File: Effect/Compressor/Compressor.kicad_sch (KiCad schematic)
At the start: 46 parts, among them J1 Conn_01x04_Pin, J2 Conn_01x04_Pin, Q1 DMMT5551, Q2 MMBF5103, Q3 DMMT5551, Q4 MMBF5103

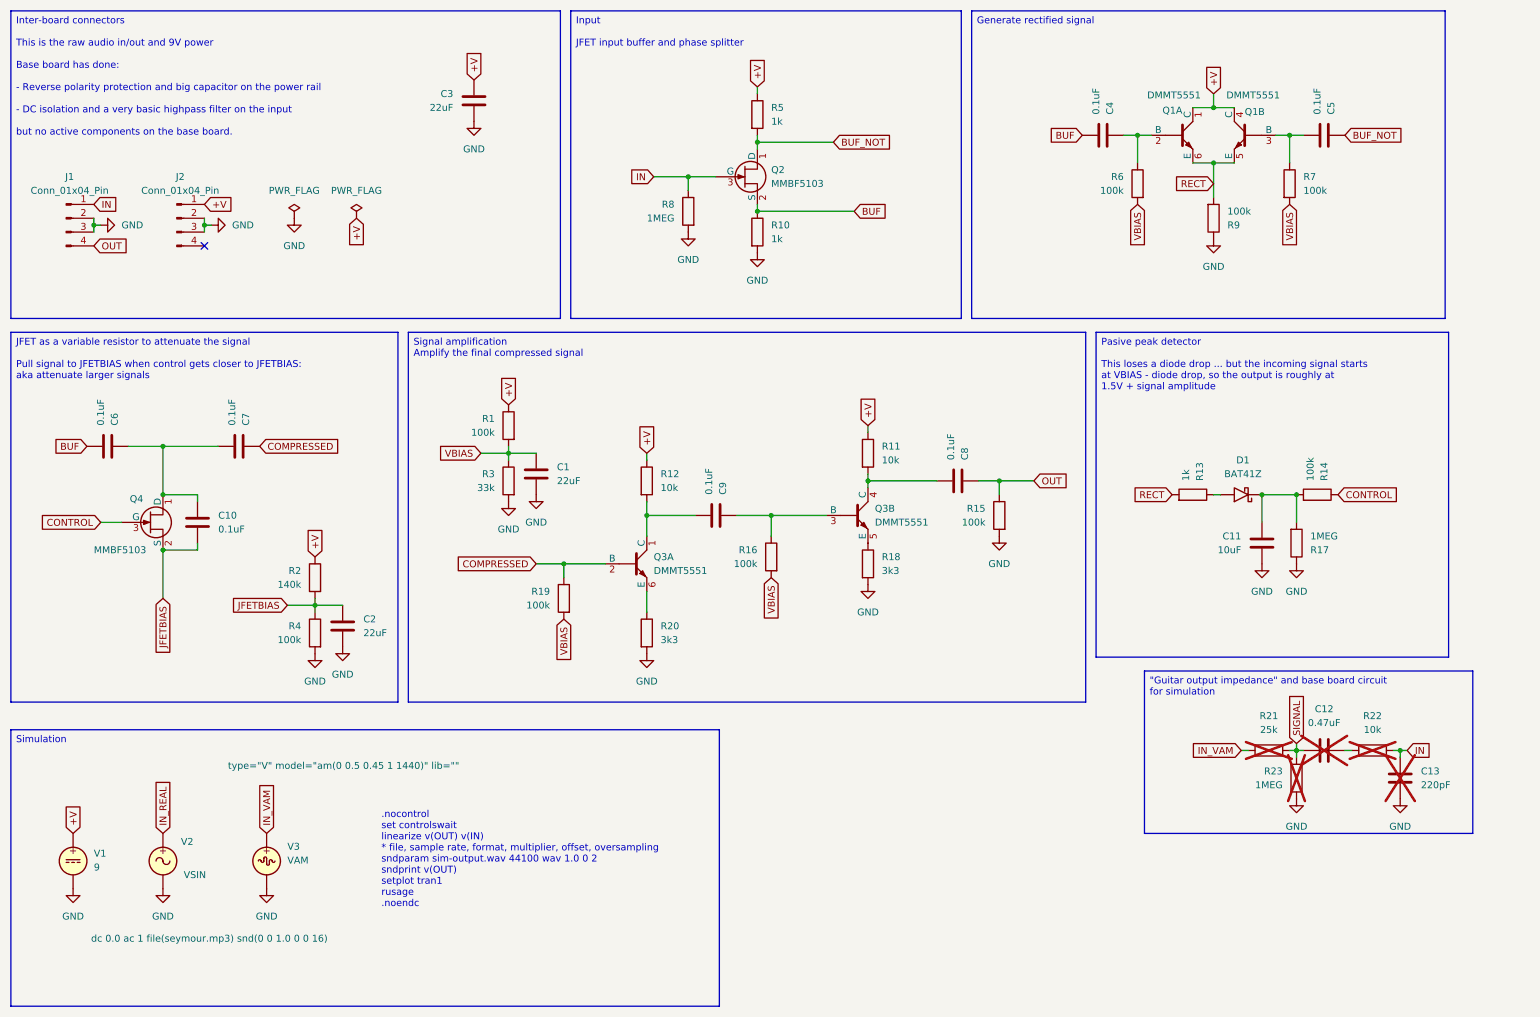
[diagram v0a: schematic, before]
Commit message: Add volume and level pots for compressor
The level pot might make the compressor able to deal with the reality of
JFET variability, at least within reason.

And obviously also in theory then allow people to actually set the level
at which things compress.

It's worth noting that the compression level is set purely based on the
input level. That's really stupid, since it really should be based on
feedback from the *output*, not the input. So high input levels might
then end up compressing to the point that the end result is less than
where medium input levels would have been.

But hey, if this things works even that well, that would be a small
miracle. The much more likely situation is that it will noisy, distort
horribly and not match my simulations at all.

My previous attempts at this do not instill confidence.

So I'll worry about smarter feedback when - and if - I ever get to that
bridge.

This also starts on the PCB layout. No components placed yet, just the
skeleton board with pots and connectors. But it's at the point where I
actually want to know if any of this works in reality, so...

Signed-off-by: Linus Torvalds <torvalds@linux-foundation.org>
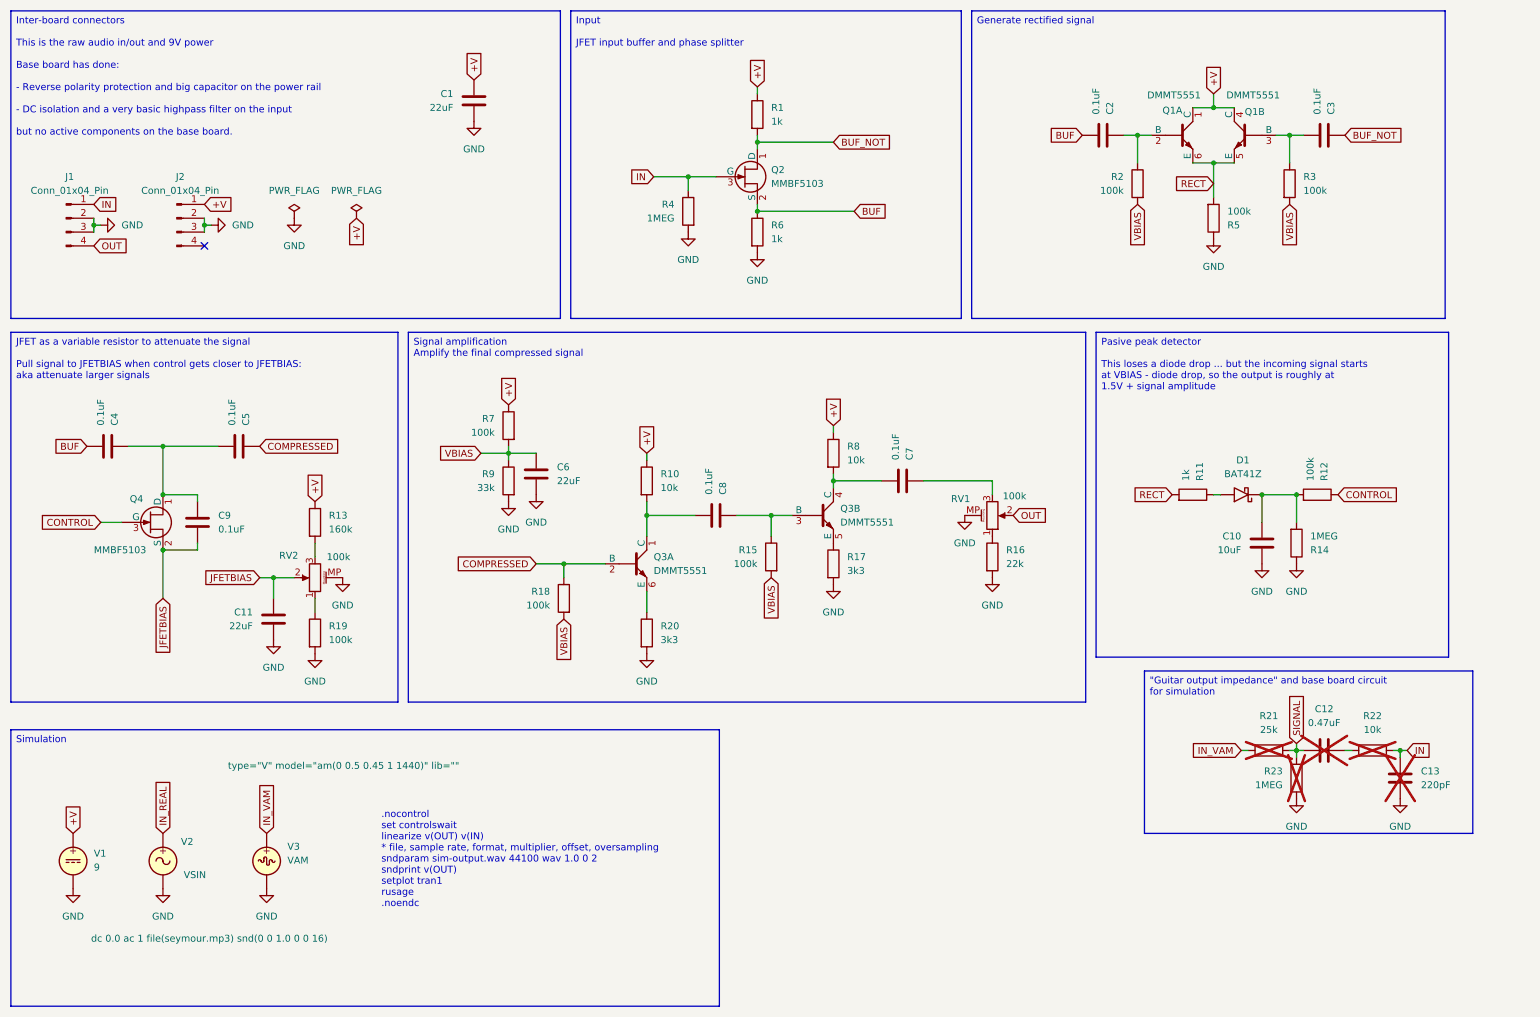
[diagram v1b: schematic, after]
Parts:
- removed R15: 100k, Resistor_SMD:R_0805_2012Metric, symbol Device:R
- added R16: 22k, Resistor_SMD:R_0805_2012Metric, symbol Device:R
- added RV1, RV2: 100k, Mylib:Potentiometer_9mm_MP, symbol Device:R_Potentiometer_MountingPin
- C2: renamed from C4; footprint Capacitor_SMD:C_1206_3216Metric -> Mylib:C_0704_1810Metric
- C3: renamed from C5; footprint Capacitor_SMD:C_1206_3216Metric -> Mylib:C_0704_1810Metric
- C4: renamed from C6; footprint Capacitor_SMD:C_1206_3216Metric -> Mylib:C_0704_1810Metric
- C5: renamed from C7; footprint Capacitor_SMD:C_1206_3216Metric -> Mylib:C_0704_1810Metric
- C7: renamed from C8; footprint Capacitor_SMD:C_1206_3216Metric -> Mylib:C_0704_1810Metric
- C8: renamed from C9; footprint Capacitor_SMD:C_1206_3216Metric -> Mylib:C_0704_1810Metric
- C9: renamed from C10; footprint Capacitor_SMD:C_1206_3216Metric -> Mylib:C_0704_1810Metric
- R13: renamed from R2; value 140k -> 160k
- renumbered C3 to C1, C11 to C10, C2 to C11, C1 to C6, R5 to R1, R12 to R10, R13 to R11, R14 to R12, R17 to R14, R16 to R15, R18 to R17, R19 to R18, R4 to R19, R6 to R2, R7 to R3, R8 to R4, R9 to R5, R10 to R6, R1 to R7, R11 to R8, R3 to R9
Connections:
- net GND: now also R16.2, RV1.MP (MountPin), RV2.MP (MountPin)
- net JFETBIAS: now also RV2.2; no longer R13.2, R19.1
- net OUT: now also RV1.2; no longer C7.1
- new net: R16.1, RV1.1
- new net: R19.1, RV2.1
- new net: R13.2, RV2.3
- new net: C7.1, RV1.3
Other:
- moved on the sheet: C11, C7, Q3B, R13, R17, R8

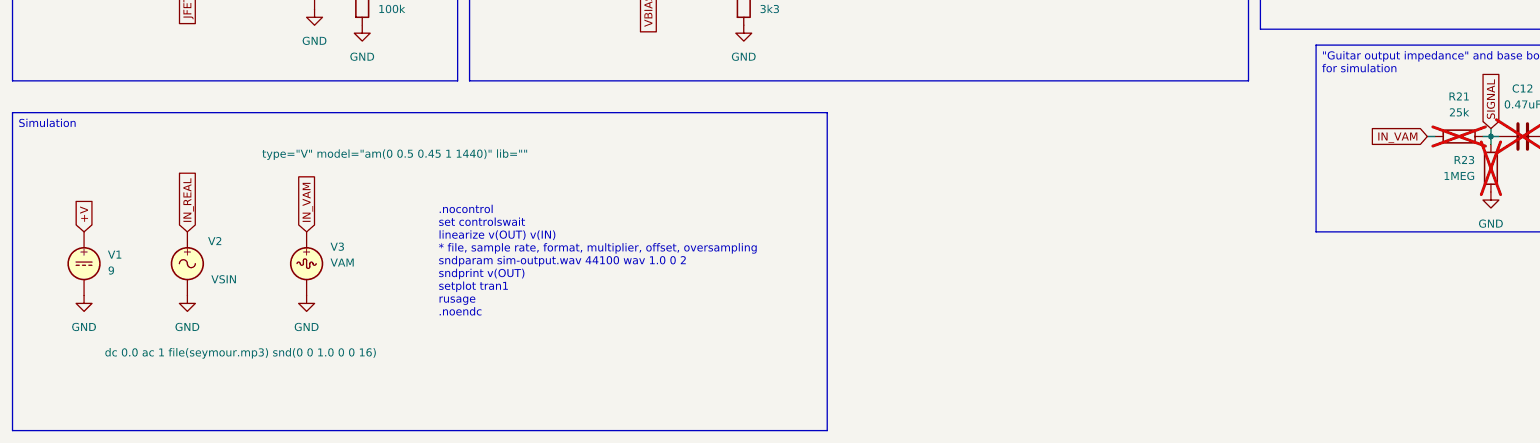
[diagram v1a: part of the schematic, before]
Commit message: Add triangle wave for compressor testing
Because of how this odd "JFET as a voltage-controlled resistor in
parallel with a capacitor" circuit works, the whole ngspice AC signal
analysis doesn't work for this at all. Which limits me to just the
transient analysis.

So to do a poor-man's frequency sweep kind of thing, by using a 125Hz
triangle wave as an input and seeing how it distorts.

Does that show distortion? It sure does.

The thinking is that it's kind of a capacitor version of a resistive
T-network, with the reactance of the capacitors all frequency-dependent
in the same way (so scaling up and down together).

But then the JFET ends up being a non-frequency-dependent resistance
pulling the signal to ground, so now low frequencies are fundamentally
attenuated more than high frequencies (because low frequencies see more
reactance through the capacitors that aren't being bypassed with the
JFET).

And even *without* that JFET interaction, the capacitors obviously then
interact with the following resistors, so it all ends up acting like
highpass filter

Still, it acts better than any other circuit I've come up with. That's
not saying a lot, I know.

I think the frequency behavior can be improved on by making the caps
bigger - but I'm limited to 0.47uF as long as I want to use the C0G
MLCCs I have for the signal path.

But some distortion is inevitable, and this might just not be great for
bass guitar. So *IF* this circuit actually works, I suspect I'll just
have to play up the distortion as giving the sound "character".

I suspect the more likely scenario is that this will be just another
nasty-sounding thing.

Signed-off-by: Linus Torvalds <torvalds@linux-foundation.org>
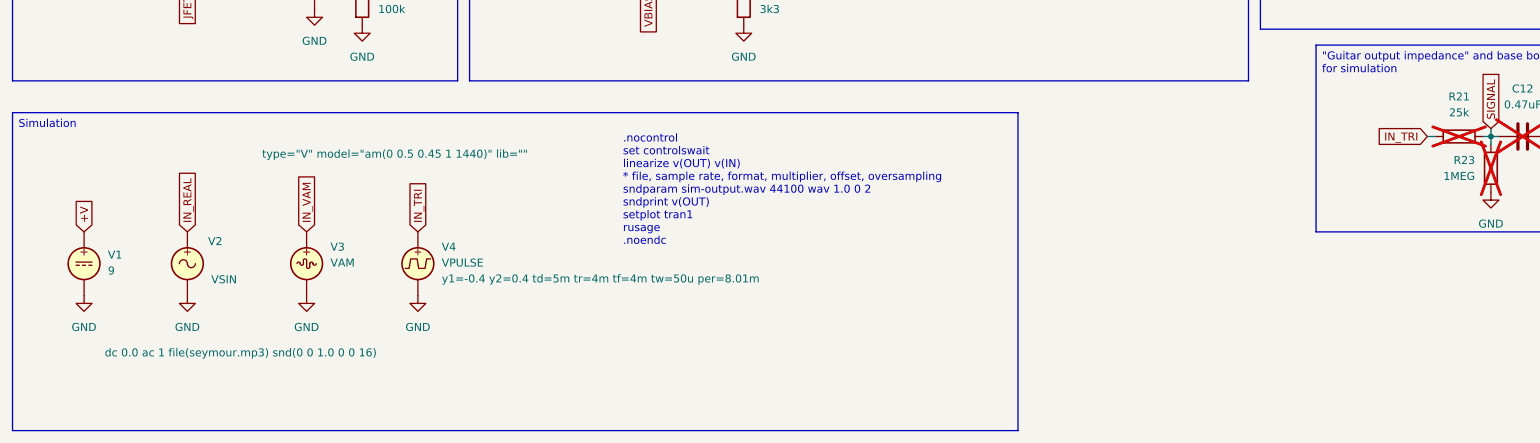
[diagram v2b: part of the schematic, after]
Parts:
- added V4: VPULSE, symbol Simulation_SPICE:VPULSE
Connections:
- net GND: now also V4.2
- net IN_VAM: no longer R21.1
- new net IN_TRI: R21.1, V4.1
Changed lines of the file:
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@@
 	(text ".nocontrol\nset controlswait\nlinearize v(OUT) v(IN)\n* file, sample rate, format, multiplier, offset, oversampling\nsndparam sim-output.wav 44100 wav 1.0 0 2\nsndprint v(OUT)\nsetplot tran1\nrusage\n.noendc\n"
 		(exclude_from_sim no)
-		(at 82.042 169.926 0)
+		(at 111.506 158.496 0)
 		(effects
 			(font
@@
 		(exclude_from_sim no)
 		(at 13.97 146.05 0)
-		(size 130.175 50.8)
+		(size 160.655 50.8)
 		(margins 0.9525 0.9525 0.9525 0.9525)
 		(stroke
@@
 		)
 	)
-	(global_label "IN_VAM"
+	(global_label "IN_TRI"
 		(shape input)
 		(at 240.03 149.86 180)
@@
 		)
 		(property "Intersheetrefs" "${INTERSHEET_REFS}"
-			(at 230.5133 149.86 0)
+			(at 231.2995 149.86 0)
 			(hide yes)
 			(effects
@@
 		)
 	)
+	(global_label "IN_TRI"
+		(shape input)
+		(at 78.74 165.1 90)
+		(fields_autoplaced yes)
+		(effects
+			(font
+				(size 1.27 1.27)
+			)
+			(justify left)
+		)
+		(property "Intersheetrefs" "${INTERSHEET_REFS}"
+			(at 78.74 156.3695 90)
+			(hide yes)
+			(effects
+				(font
+					(size 1.27 1.27)
+				)
+				(justify left)
+			)
+		)
+	)
 	(global_label "VBIAS"
 		(shape input)
@@
 	)
 	(symbol
+		(lib_id "Simulation_SPICE:VPULSE")
+		(at 78.74 170.18 0)
+		(unit 1)
+		(exclude_from_sim no)
+		(in_bom yes)
+		(on_board yes)
+		(dnp no)
+		(fields_autoplaced yes)
+		(property "Reference" "V4"
+			(at 82.55 167.5101 0)
+			(effects
+				(font
+					(size 1.27 1.27)
+				)
+				(justify left)
+			)
+		)
+		(property "Value" "VPULSE"
+			(at 82.55 170.0501 0)
+			(effects
+				(font
+					(size 1.27 1.27)
+				)
+				(justify left)
+			)
+		)
+		(property "Footprint" ""
+			(at 78.74 170.18 0)
+			(hide yes)
+			(effects
+				(font
+					(size 1.27 1.27)
+				)
+			)
+		)
+		(property "Datasheet" "https://ngspice.sourceforge.io/docs/ngspice-html-manual/manual.xhtml#sec_Independent_Sources_for"
+			(at 78.74 170.18 0)
+			(hide yes)
+			(effects
+				(font
+					(size 1.27 1.27)
+				)
+			)
+		)
+		(property "Description" "Voltage source, pulse"
+			(at 78.74 170.18 0)
+			(hide yes)
+			(effects
+				(font
+					(size 1.27 1.27)
+				)
+			)
+		)
+		(property "Sim.Pins" "1=+ 2=-"
+			(at 78.74 170.18 0)
+			(hide yes)
+			(effects
+				(font
+					(size 1.27 1.27)
+				)
+			)
+		)
+		(property "Sim.Type" "PULSE"
+			(at 78.74 170.18 0)
+			(hide yes)
+			(effects
+				(font
+					(size 1.27 1.27)
+				)
+			)
+		)
+		(property "Sim.Device" "V"
+			(at 78.74 170.18 0)
+			(hide yes)
+			(effects
+				(font
+					(size 1.27 1.27)
+				)
+				(justify left)
+			)
+		)
+		(property "Sim.Params" "y1=-0.4 y2=0.4 td=5m tr=4m tf=4m tw=50u per=8.01m"
+			(at 82.55 172.5901 0)
+			(effects
+				(font
+					(size 1.27 1.27)
+				)
+				(justify left)
+			)
+		)
+		(pin "1"
+		)
+		(pin "2"
+		)
+		(instances
+			(project ""
+				(path "/9e337e0b-885b-4d2b-99a2-62cdd082c615"
+					(reference "V4")
+					(unit 1)
+				)
+			)
+		)
+	)
+	(symbol
 		(lib_id "power:GND")
 		(at 30.48 53.34 90)
@@
 					(unit 1)
 				)
+			)
+		)
+	)
+	(symbol
+		(lib_id "power:GND")
+		(at 78.74 175.26 0)
+		(unit 1)
+		(exclude_from_sim no)
+		(in_bom yes)
+		(on_board yes)
+		(dnp no)
+		(fields_autoplaced yes)
+		(property "Reference" "#PWR024"
+			(at 78.74 181.61 0)
+			(hide yes)
+			(effects
+				(font
+					(size 1.27 1.27)
+				)
+			)
+		)
+		(property "Value" "GND"
+			(at 78.74 180.34 0)
+			(effects
+				(font
+					(size 1.27 1.27)
+				)
+			)
+		)
+		(property "Footprint" ""
+			(at 78.74 175.26 0)
+			(hide yes)
+			(effects
+				(font
+					(size 1.27 1.27)
+				)
+			)
+		)
+		(property "Datasheet" ""
+			(at 78.74 175.26 0)
+			(hide yes)
+			(effects
+				(font
+					(size 1.27 1.27)
+				)
+			)
+		)
+		(property "Description" "Power symbol creates a global label with name \"GND\" , ground"
+			(at 78.74 175.26 0)
+			(hide yes)
+			(effects
+				(font
+					(size 1.27 1.27)
+				)
+			)
+		)
+		(pin "1"
+		)
+		(instances
+			(project "Compressor"
+				(path "/9e337e0b-885b-4d2b-99a2-62cdd082c615"
+					(reference "#PWR024")
+					(unit 1)
+				)
